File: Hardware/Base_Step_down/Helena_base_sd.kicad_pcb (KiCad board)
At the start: 2 copper layers, 38 x 18 mm, 59 parts, among them IC1 ATTINY85-S, P1 CONN_01X01, P2 CONN_01X01, P3 CONN_01X01, P4 CONN_01X06, P5 CONN_01X01, P6 CONN_01X01, P7 CONN_01X01, P8 CONN_01X01, Q1 BC857C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

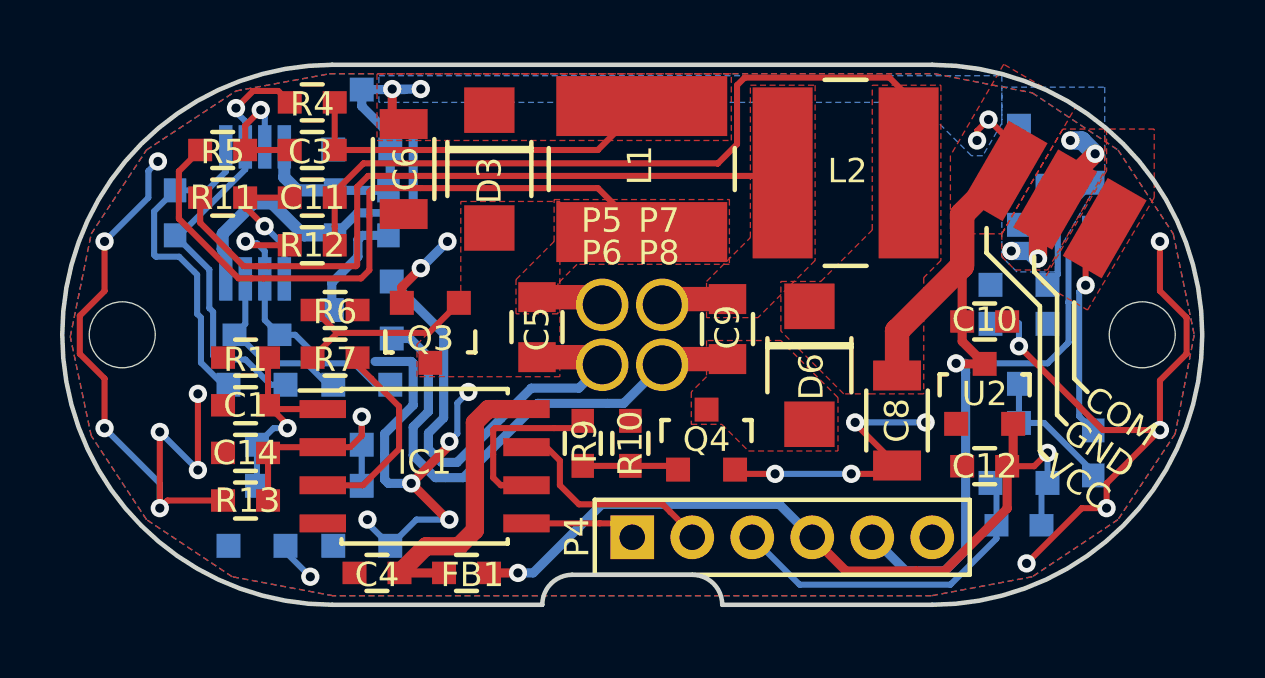
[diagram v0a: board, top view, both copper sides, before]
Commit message: Hardware update for better compatibility with KD2 style lights
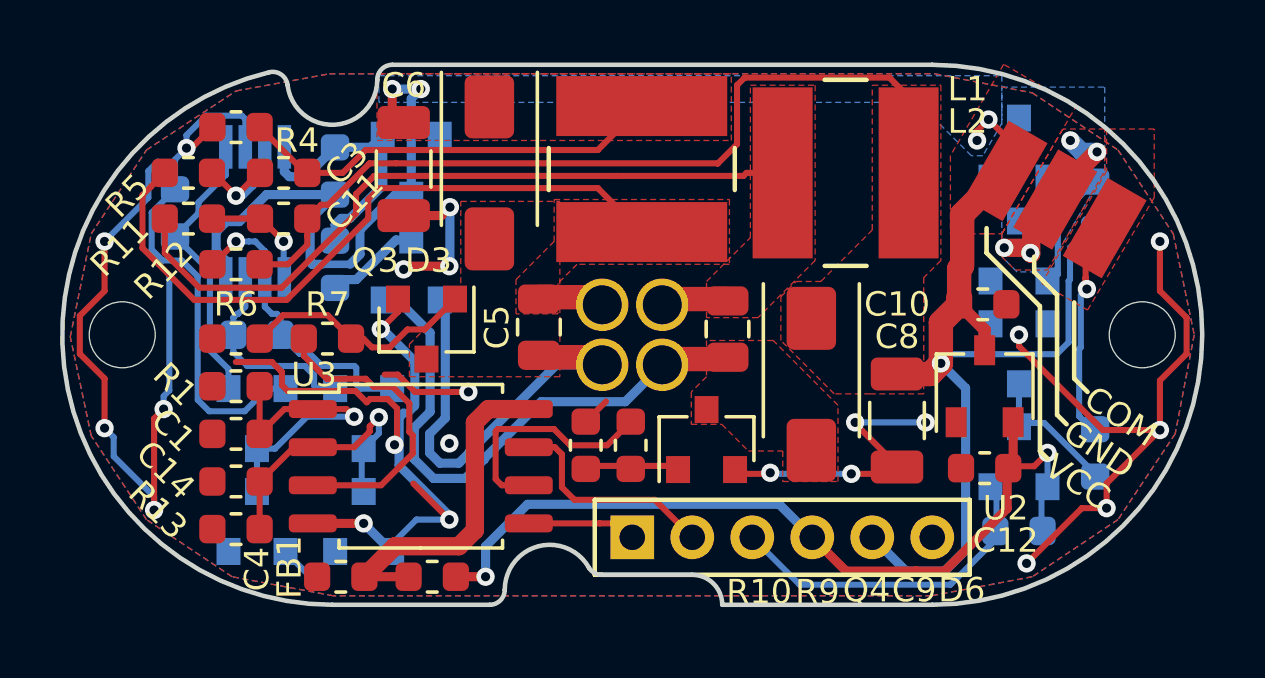
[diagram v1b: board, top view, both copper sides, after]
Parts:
- removed IC1: ATTINY85-S, rt_Housings_SOIC:SOIC-8_5.29x4.9mm_Pitch1.27mm
- added U3: ATTINY85-S, Package_SO:SOIC-8_5.23x5.23mm_P1.27mm, F.Cu at (43.0, 154.4)
- C1, C10, C11, C12, C13, C14, C2, C3, C4, C7: footprint rt_device:C_0603_THERMaL_RELIEF -> Capacitor_SMD:C_0603_1608Metric
- C5, C9: footprint Capacitors_SMD:C_0805 -> Capacitor_SMD:C_0805_2012Metric
- C6, C8: footprint Capacitors_SMD:C_1206 -> Capacitor_SMD:C_1206_3216Metric
- D1, D2, D4, D5, D7, Q1, Q2, Q3, Q4, Q5: footprint TO_SOT_Packages_SMD:SOT-23 -> Package_TO_SOT_SMD:SOT-23
- D3, D6: footprint rt_diodes:SMA -> rt_diodes:D_SMA
- FB1: footprint rt_device:C_0603_THERMaL_RELIEF -> Inductor_SMD:L_0603_1608Metric
- Q6, Q7: footprint footprints:SOT-23 -> Package_TO_SOT_SMD:SOT-23
- R1, R10, R11, R12, R13, R14, R2, R3, R4, R5, R6, R7, R8, R9: footprint rt_device:C_0603_THERMaL_RELIEF -> Resistor_SMD:R_0603_1608Metric
- U1: footprint Housings_SSOP:MSOP-8_3x3mm_Pitch0.65mm -> Package_SO:MSOP-8_3x3mm_P0.65mm
- U2: footprint TO_SOT_Packages_SMD:SOT-23 -> Package_TO_SOT_SMD:SOT-23W
- moved R6 3.44 mm to (36.8, 150.1), turned to 0 degrees
- moved R4 2.67 mm to (36.8, 143.1)
- moved R12 2.62 mm to (36.8, 147.7)
- moved R8 2.47 mm to (40.1, 147.7)
- moved D4 2.25 mm to (42.6, 144.3), turned to 270 degrees
- moved D5 2.12 mm to (42.6, 147.8), turned to 90 degrees
- moved R9 1.60 mm to (49.9, 153.7)
- moved R10 1.49 mm to (48.5, 153.7)
- moved C7 1.40 mm to (40.1, 144.5)
- moved R5 1.37 mm to (35.2, 144.6)
- moved R11 1.34 mm to (35.2, 146.1)
- moved C3 1.22 mm to (38.4, 144.6)
- moved C4 1.21 mm to (40.3, 158.1)
- moved C11 1.18 mm to (38.4, 146.1)
- moved FB1 1.15 mm to (43.3, 158.1)
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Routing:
- net GND: track 74.1 -> 86.3 mm, vias 24 -> 22
- net VPP: track 92.9 -> 96.9 mm
- net /SDL_CURR: track 7.11 -> 10.2 mm
- net Net-(C2-Pad1): track 15.0 -> 18.1 mm
- net /SDL_SW: track 7.14 -> 10.2 mm
- net /OPAMP-: track 6.05 -> 9.09 mm
- net /SDR_SW: track 5.91 -> 7.87 mm
- net +3V3: track 26.9 -> 28.7 mm
- net Net-(C2-Pad2): track 11.1 -> 9.50 mm
- net Net-(C9-Pad2): track 17.4 -> 18.8 mm
- net /SDR_CURR: track 7.89 -> 9.17 mm
- net Net-(C4-Pad1): track 10.1 -> 11.3 mm
- net Net-(C5-Pad2): track 16.1 -> 14.9 mm
- net Net-(C11-Pad2): track 5.10 -> 3.96 mm
- net Net-(Q3-Pad1): track 6.89 -> 8.00 mm
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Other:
- outline, holes or cut-outs redrawn
- net class Default: clearance 0.1524 -> 0.2032
- rule pad_to_mask_clearance: 0.2 -> 0.05
- rule trace_clearance: 0.1524 -> 0.2032
- board text added: "+"
- board text added: "-"
- board text added: "Dual 3.0A Step Down Converter Rev 2.3"
- board text added: "RT1908"
- board text removed: "Anode"
- board text removed: "Cathode"
- board text removed: "Dual 3.0A Step Down Converter Rev 2.2"
- board text removed: "RT1702"
